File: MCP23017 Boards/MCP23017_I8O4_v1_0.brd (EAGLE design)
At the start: 90 x 90 mm, 65 parts, among them IC5 MCP23017SP, X4 057-016-0

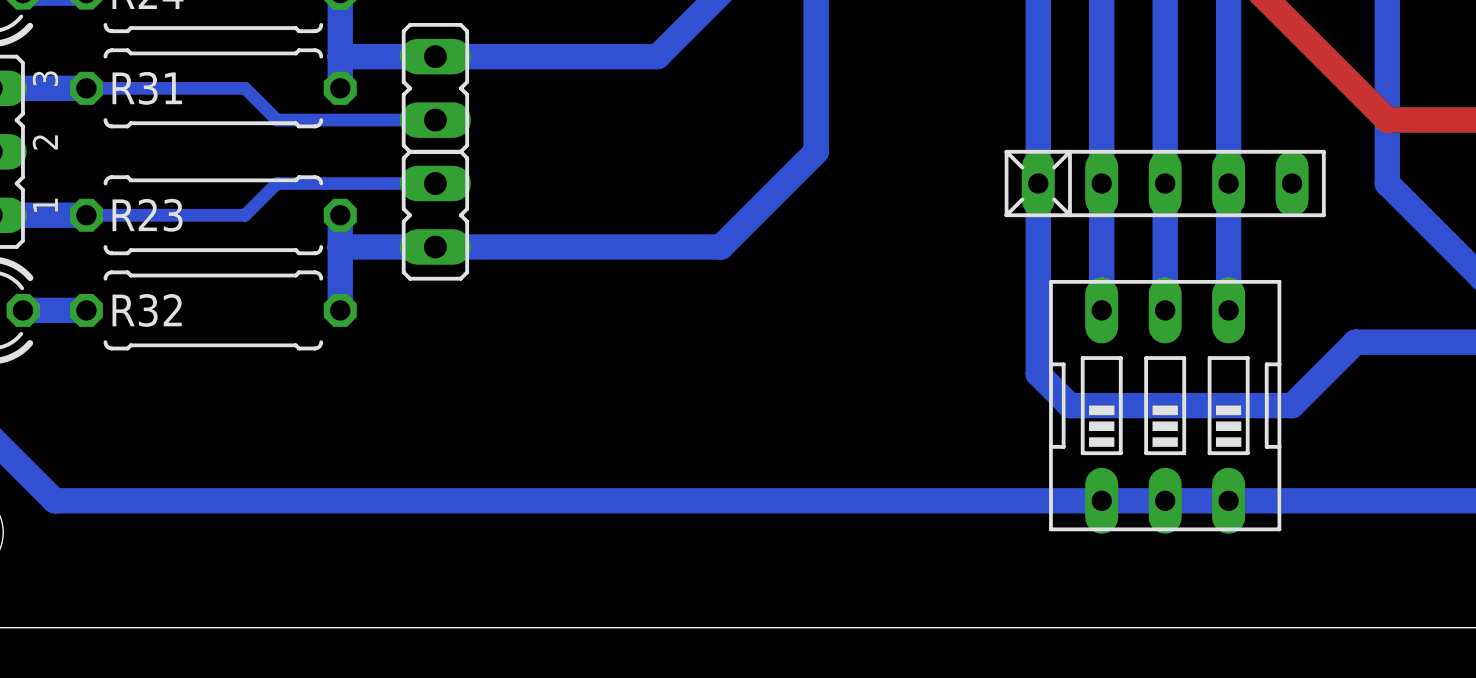
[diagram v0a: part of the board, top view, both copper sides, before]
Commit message: Update MCP23017_I8O4_v1_0.brd
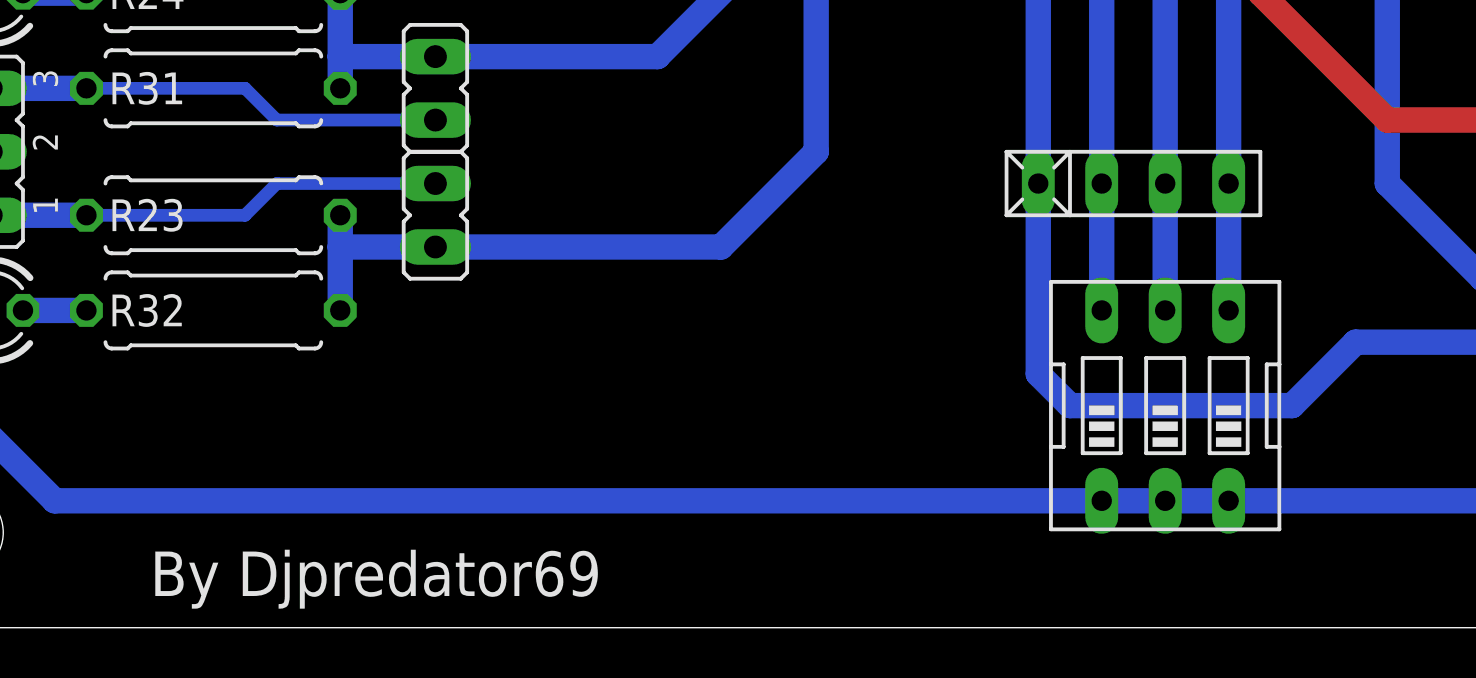
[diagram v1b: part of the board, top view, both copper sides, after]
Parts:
- RN2: device resistor-net:RN-5 -> resistor-net_edit:RN-3
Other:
- board text added: "By Djpredator69"
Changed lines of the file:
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@@
 <text x="5.08" y="81.28" size="3.81" layer="25" rot="R90">1</text>
 <text x="5.08" y="7.62" size="3.81" layer="25" rot="R90">4</text>
+<text x="11.43" y="1.27" size="1.778" layer="25">By Djpredator69</text>
 </plain>
 <attributes>
@@
 <attribute name="VALUE" x="47.498" y="2.286" size="1.27" layer="27" ratio="10"/>
 </element>
-<element name="RN2" library="resistor-net" library_urn="urn:adsk.eagle:library:343" package="RN-5" package3d_urn="urn:adsk.eagle:package:24976/1" value="" x="52.07" y="17.78" smashed="yes">
+<element name="RN2" library="resistor-net_edit" package="RN-3" value="" x="52.07" y="17.78" smashed="yes">
 <attribute name="MF" value="" x="52.07" y="17.78" size="1.778" layer="27" display="off"/>
 <attribute name="MPN" value="" x="52.07" y="17.78" size="1.778" layer="27" display="off"/>
